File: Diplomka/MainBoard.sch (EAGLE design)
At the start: 44 parts, among them K1 ARK550/2, Q1 AP2012P3C-P22, Q2 BC817-40LT1SMD, Q3 SS8050-G, Q4 SS8050-G, U1 ESP32-WROOM-32, U2 AMS1117-3.3

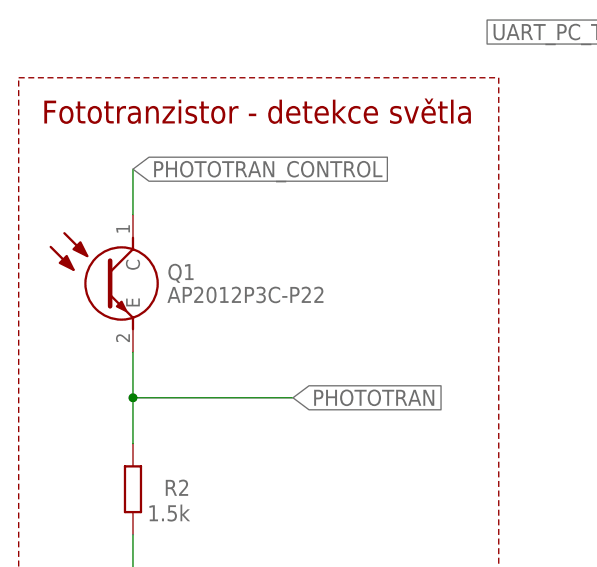
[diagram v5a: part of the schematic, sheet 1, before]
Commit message: Přidán rozumný fototranzistor.
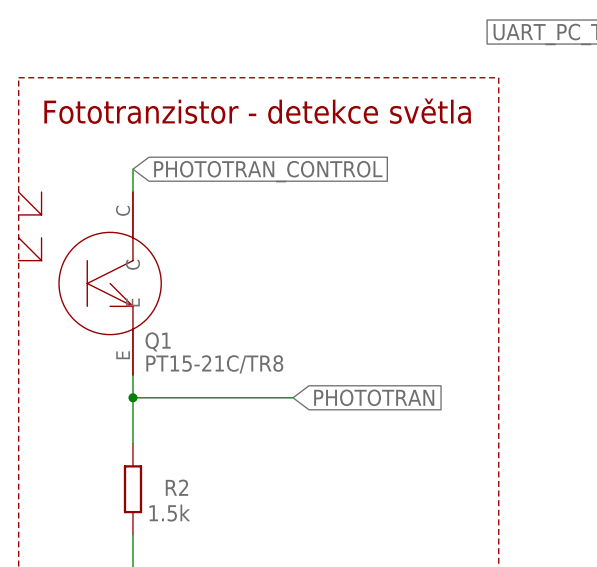
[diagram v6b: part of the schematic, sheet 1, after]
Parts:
- Q1: value AP2012P3C-P22 -> PT15-21C/TR8; device SamacSys_Parts:AP2012P3C-P22 -> myParts:PT15-21C/TR8
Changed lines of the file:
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@@
 <part name="GND1" library="supply1" library_urn="urn:adsk.eagle:library:371" deviceset="GND" device=""/>
 <part name="R2" library="rcl" library_urn="urn:adsk.eagle:library:334" deviceset="R-EU_" device="R0805" package3d_urn="urn:adsk.eagle:package:23553/2" value="1.5k"/>
-<part name="Q1" library="SamacSys_Parts" deviceset="AP2012P3C-P22" device=""/>
+<part name="Q1" library="myParts" deviceset="PT15-21C/TR8" device=""/>
 <part name="GND2" library="supply1" library_urn="urn:adsk.eagle:library:371" deviceset="GND" device=""/>
 <part name="U$1" library="Sensors_PIR_Lux" deviceset="HC-SR501" device=""/>
@@
 <attribute name="VALUE" x="26.67" y="28.702" size="1.778" layer="96" rot="R180"/>
 </instance>
-<instance part="Q1" gate="G$1" x="20.32" y="60.96" smashed="yes">
-<attribute name="NAME" x="24.13" y="54.61" size="1.778" layer="95" align="center-left"/>
-<attribute name="VALUE" x="24.13" y="52.07" size="1.778" layer="96" align="center-left"/>
+<instance part="Q1" gate="G$1" x="17.78" y="53.34" smashed="yes">
+<attribute name="NAME" x="21.59" y="46.99" size="1.778" layer="95" align="center-left"/>
+<attribute name="VALUE" x="21.59" y="44.45" size="1.778" layer="96" align="center-left"/>
 </instance>
 <instance part="GND2" gate="1" x="20.32" y="17.78" smashed="yes">
@@
 <wire x1="20.32" y1="35.56" x2="20.32" y2="40.64" width="0.1524" layer="91"/>
 <pinref part="Q1" gate="G$1" pin="E"/>
-<wire x1="20.32" y1="40.64" x2="20.32" y2="45.72" width="0.1524" layer="91"/>
+<wire x1="20.32" y1="40.64" x2="20.32" y2="43.18" width="0.1524" layer="91"/>
 <junction x="20.32" y="40.64"/>
 </segment>
@@
 <segment>
 <pinref part="Q1" gate="G$1" pin="C"/>
-<wire x1="20.32" y1="60.96" x2="20.32" y2="66.04" width="0.1524" layer="91"/>
+<wire x1="20.32" y1="63.5" x2="20.32" y2="66.04" width="0.1524" layer="91"/>
 <label x="20.32" y="66.04" size="1.778" layer="95" xref="yes"/>
 </segment>

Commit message: Udělána objednávka.
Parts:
- Q2: value BC817-40LT1SMD -> SS8050-G; device transistor-npn:BC817-40LT1SMD -> SS8050-G:SS8050-G
- R16, R17: value (none) -> 10k
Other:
- moved on the sheet: Q2
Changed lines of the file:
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@@
 <part name="U$3" library="myParts" deviceset="GY4466" device=""/>
 <part name="U$4" library="myParts" deviceset="BUZZER" device=""/>
-<part name="Q2" library="transistor-npn" library_urn="urn:adsk.eagle:library:398" deviceset="BC817*" device="SMD" package3d_urn="urn:adsk.eagle:package:28748/2" technology="-40LT1"/>
+<part name="Q2" library="SS8050-G" deviceset="SS8050-G" device=""/>
 <part name="GND6" library="supply1" library_urn="urn:adsk.eagle:library:371" deviceset="GND" device=""/>
 <part name="R8" library="rcl" library_urn="urn:adsk.eagle:library:334" deviceset="R-EU_" device="R0805" package3d_urn="urn:adsk.eagle:package:23553/2" value="1k"/>
@@
 <part name="Q3" library="SS8050-G" deviceset="SS8050-G" device=""/>
 <part name="Q4" library="SS8050-G" deviceset="SS8050-G" device=""/>
-<part name="R16" library="rcl" library_urn="urn:adsk.eagle:library:334" deviceset="R-EU_" device="R0805" package3d_urn="urn:adsk.eagle:package:23553/2"/>
-<part name="R17" library="rcl" library_urn="urn:adsk.eagle:library:334" deviceset="R-EU_" device="R0805" package3d_urn="urn:adsk.eagle:package:23553/2"/>
+<part name="R16" library="rcl" library_urn="urn:adsk.eagle:library:334" deviceset="R-EU_" device="R0805" package3d_urn="urn:adsk.eagle:package:23553/2" value="10k"/>
+<part name="R17" library="rcl" library_urn="urn:adsk.eagle:library:334" deviceset="R-EU_" device="R0805" package3d_urn="urn:adsk.eagle:package:23553/2" value="10k"/>
 </parts>
 <sheets>
@@
 <segment>
 <pinref part="Q2" gate="G$1" pin="E"/>
-<wire x1="142.24" y1="20.32" x2="142.24" y2="17.78" width="0.1524" layer="91"/>
+<wire x1="149.86" y1="17.78" x2="142.24" y2="17.78" width="0.1524" layer="91"/>
 <pinref part="GND6" gate="1" pin="GND"/>
 </segment>
@@
 <pinref part="Q2" gate="G$1" pin="C"/>
 <pinref part="U$4" gate="G$1" pin="-"/>
-<wire x1="142.24" y1="30.48" x2="142.24" y2="33.02" width="0.1524" layer="91"/>
+<wire x1="149.86" y1="33.02" x2="142.24" y2="33.02" width="0.1524" layer="91"/>
 </segment>
 </net>
@@
 <pinref part="R8" gate="G$1" pin="2"/>
 <pinref part="Q2" gate="G$1" pin="B"/>
-<wire x1="134.62" y1="25.4" x2="137.16" y2="25.4" width="0.1524" layer="91"/>
-</segment>
-</net>
+<wire x1="134.62" y1="25.4" x2="139.7" y2="25.4" width="0.1524" layer="91"/>
+</segment>
+</net>

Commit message: WIP
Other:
- note added: "SD8942"
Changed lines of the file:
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@@
 <wire x1="2.54" y1="254" x2="2.54" y2="172.72" width="0.1524" layer="94" style="longdash"/>
 <text x="60.96" y="246.38" size="1.778" layer="94">Step down převodník pro 5V</text>
+<text x="43.18" y="218.44" size="1.778" layer="95">SD8942</text>
 </plain>
 <instances>
